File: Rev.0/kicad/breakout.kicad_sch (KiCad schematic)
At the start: 29 parts, among them J1 Conn_02x10_Odd_Even, J10 Conn_02x10_Odd_Even, J12 Conn_02x10_Odd_Even, J2 Conn_02x10_Odd_Even, J3 Conn_01x02, J4 Conn_01x03_Pin, J5 Conn_01x05_Pin, U1 RP2040Z, U2 PCAL6408APW, U3 PCAL6408APW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

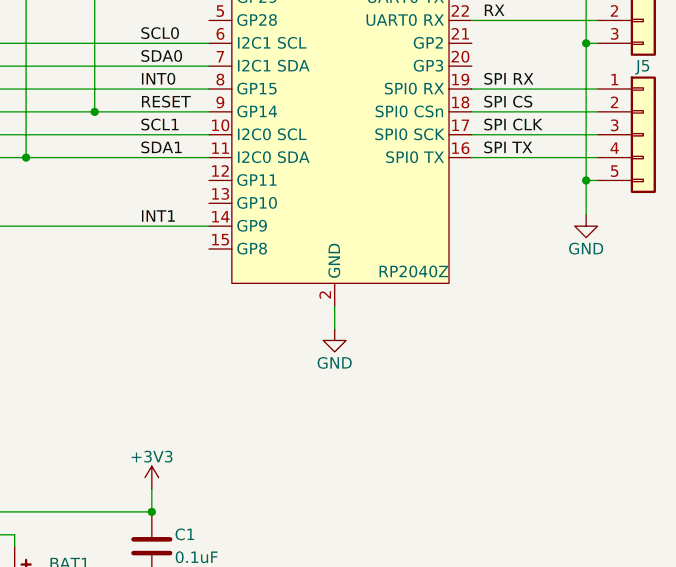
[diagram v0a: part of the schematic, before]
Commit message: Rev.0: corrected U1 to WaveShare RP2040-TINY
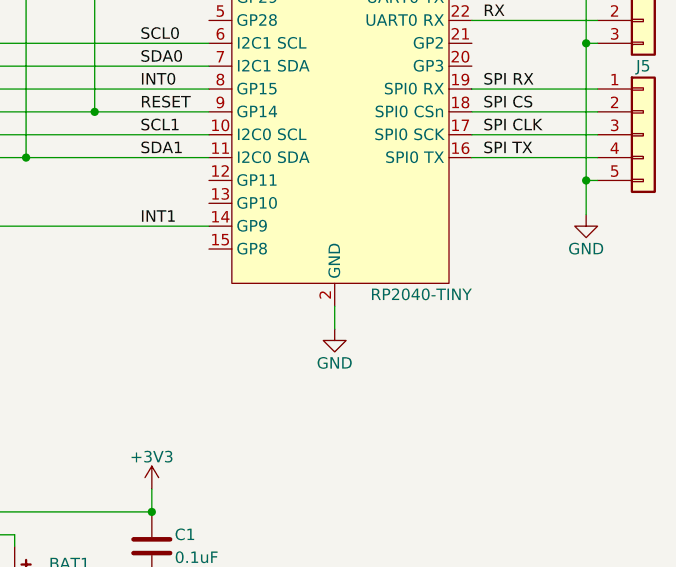
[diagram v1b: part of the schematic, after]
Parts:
- U1: value RP2040Z -> RP2040-TINY; footprint uhppoted:RP2040Z -> uhppoted:RP2040-TINY; symbol uhppoted:RP2040Z -> uhppoted:RP2040-TINY
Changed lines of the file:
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@@
     )
   )
-  (symbol (lib_id "uhppoted:RP2040Z") (at 240.03 50.8 0) (mirror y) (unit 1)
+  (symbol (lib_id "uhppoted:RP2040-TINY") (at 240.03 50.8 0) (mirror y) (unit 1)
     (in_bom yes) (on_board yes) (dnp no)
     (property "Reference" "U1" (at 231.14 27.94 0)
       (effects (font (size 1.27 1.27)) (justify left))
     )
-    (property "Value" "RP2040Z" (at 252.73 67.31 0)
+    (property "Value" "RP2040-TINY" (at 255.27 69.85 0)
       (effects (font (size 1.27 1.27)) (justify left))
     )
-    (property "Footprint" "uhppoted:RP2040Z" (at 234.0259 24.13 0)
-      (effects (font (size 1.27 1.27)) (justify left) hide)
-    )
-    (property "Datasheet" "" (at 238.76 39.37 0)
+    (property "Footprint" "uhppoted:RP2040-TINY" (at 252.73 71.12 0)
       (effects (font (size 1.27 1.27)) hide)
     )
+    (property "Datasheet" "" (at 238.76 45.72 0)
+      (effects (font (size 1.27 1.27)) hide)
+    )
